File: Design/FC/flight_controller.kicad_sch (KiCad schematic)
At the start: 43 parts, among them U1 STM32H747BIT6

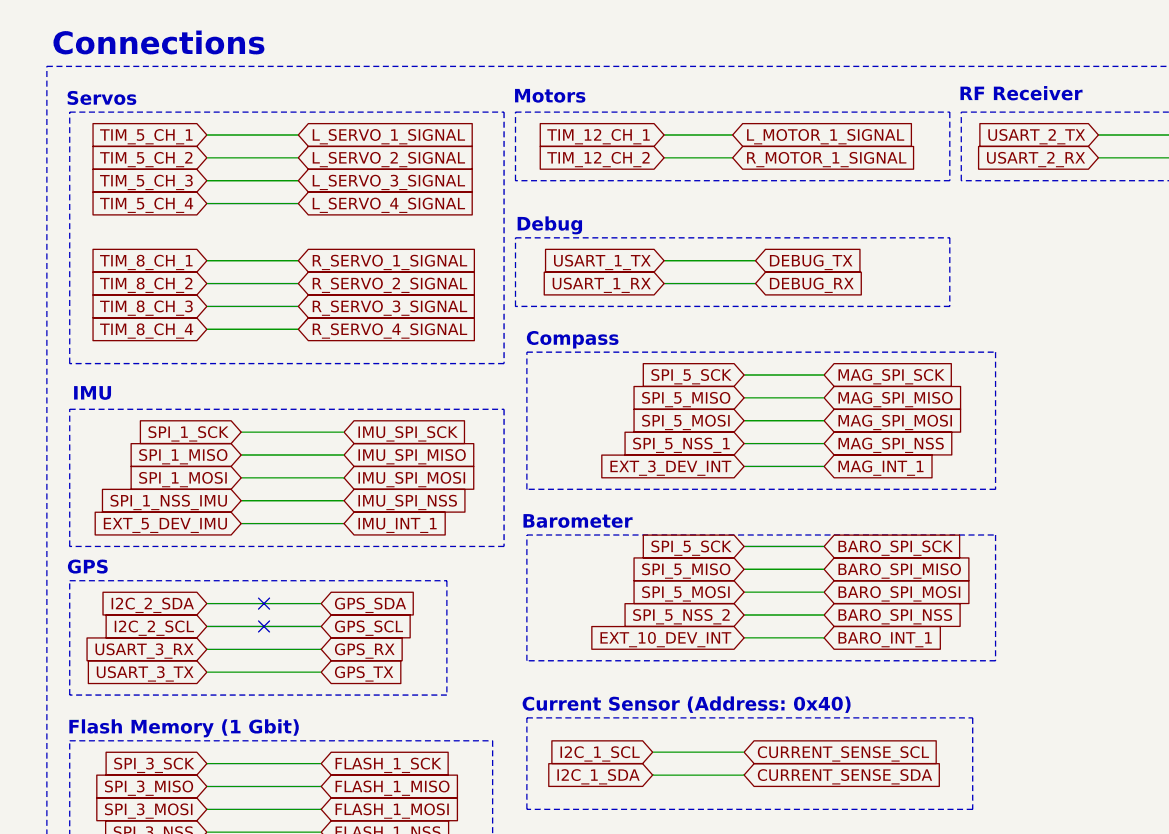
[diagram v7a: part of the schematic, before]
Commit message: extended smd pads for lga packages
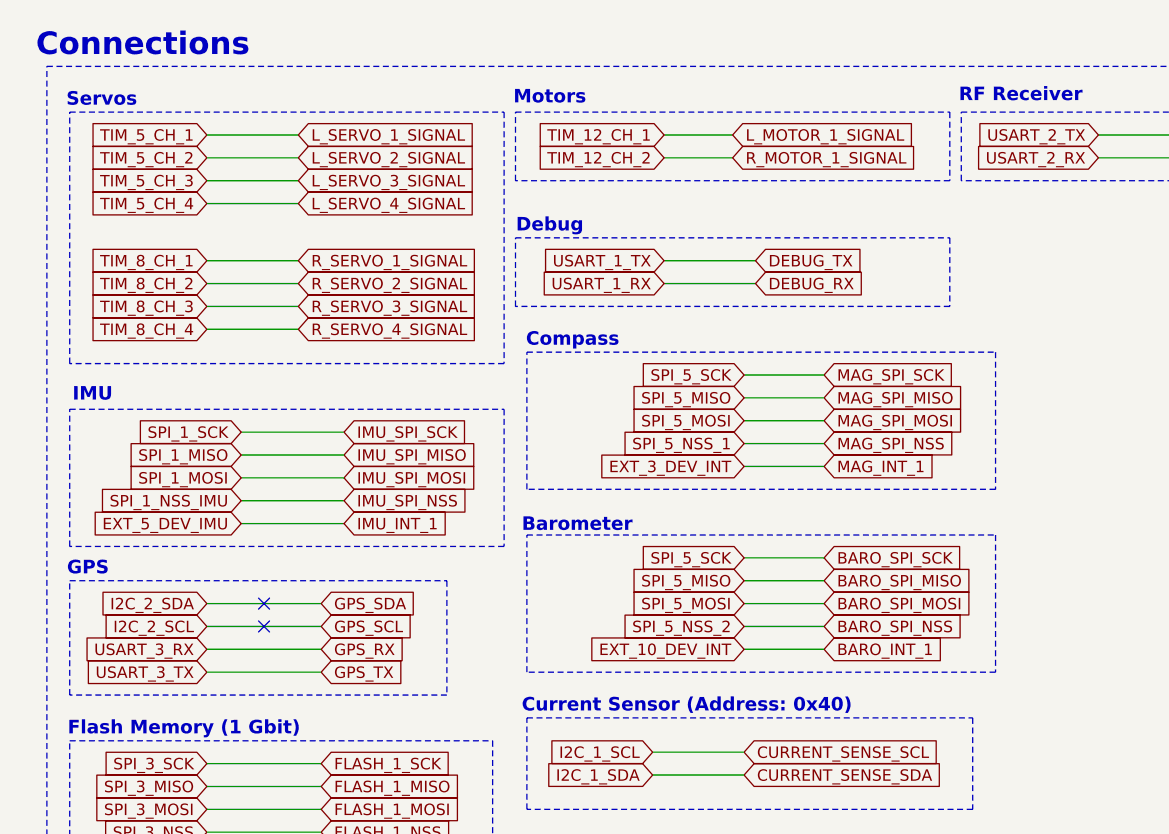
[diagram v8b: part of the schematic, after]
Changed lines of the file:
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@@
 	(rectangle
 		(start 67.31 71.12)
-		(end 119.38 85.09)
+		(end 119.38 86.36)
 		(stroke
 			(width 0)
@@
 	(text "Connections"
 		(exclude_from_sim no)
-		(at 26.416 16.764 0)
+		(at 24.638 16.764 0)
 		(effects
 			(font
@@
 	(text "Barometer"
 		(exclude_from_sim no)
-		(at 72.898 69.85 0)
+		(at 72.898 70.104 0)
 		(effects
 			(font
@@
 	(wire
 		(pts
-			(xy 91.44 74.93) (xy 100.33 74.93)
+			(xy 91.44 76.2) (xy 100.33 76.2)
 		)
 		(stroke
@@
 	(wire
 		(pts
-			(xy 91.44 72.39) (xy 100.33 72.39)
+			(xy 91.44 73.66) (xy 100.33 73.66)
 		)
 		(stroke
@@
 	(wire
 		(pts
-			(xy 91.44 80.01) (xy 100.33 80.01)
+			(xy 91.44 81.28) (xy 100.33 81.28)
 		)
 		(stroke
@@
 	(wire
 		(pts
-			(xy 91.44 77.47) (xy 100.33 77.47)
+			(xy 91.44 78.74) (xy 100.33 78.74)
 		)
 		(stroke
@@
 	(wire
 		(pts
-			(xy 91.44 82.55) (xy 100.33 82.55)
+			(xy 91.44 83.82) (xy 100.33 83.82)
 		)
 		(stroke
@@
 	(global_label "BARO_INT_1"
 		(shape input)
-		(at 100.33 82.55 0)
+		(at 100.33 83.82 0)
 		(fields_autoplaced yes)
 		(effects
@@
 		)
 		(property "Intersheetrefs" "${INTERSHEET_REFS}"
-			(at 114.3219 82.55 0)
+			(at 114.3219 83.82 0)
 			(effects
 				(font
@@
 	(global_label "BARO_SPI_SCK"
 		(shape input)
-		(at 100.33 72.39 0)
+		(at 100.33 73.66 0)
 		(fields_autoplaced yes)
 		(effects
@@
 		)
 		(property "Intersheetrefs" "${INTERSHEET_REFS}"
-			(at 117.0433 72.39 0)
+			(at 117.0433 73.66 0)
 			(effects
 				(font
@@
 	(global_label "EXT_10_DEV_INT"
 		(shape input)
-		(at 91.44 82.55 180)
+		(at 91.44 83.82 180)
 		(fields_autoplaced yes)
 		(effects
@@
 		)
 		(property "Intersheetrefs" "${INTERSHEET_REFS}"
-			(at 73.3964 82.55 0)
+			(at 73.3964 83.82 0)
 			(effects
 				(font
@@
 	(global_label "SPI_5_SCK"
 		(shape input)
-		(at 91.44 72.39 180)
+		(at 91.44 73.66 180)
 		(fields_autoplaced yes)
 		(effects
@@
 		)
 		(property "Intersheetrefs" "${INTERSHEET_REFS}"
-			(at 78.4763 72.39 0)
+			(at 78.4763 73.66 0)
 			(effects
 				(font
@@
 	(global_label "SPI_5_MISO"
 		(shape input)
-		(at 91.44 74.93 180)
+		(at 91.44 76.2 180)
 		(fields_autoplaced yes)
 		(effects
@@
 		)
 		(property "Intersheetrefs" "${INTERSHEET_REFS}"
-			(at 77.6296 74.93 0)
+			(at 77.6296 76.2 0)
 			(effects
 				(font
@@
 	(global_label "BARO_SPI_MISO"
 		(shape input)
-		(at 100.33 74.93 0)
+		(at 100.33 76.2 0)
 		(fields_autoplaced yes)
 		(effects
@@
 		)
 		(property "Intersheetrefs" "${INTERSHEET_REFS}"
-			(at 117.89 74.93 0)
+			(at 117.89 76.2 0)
 			(effects
 				(font
@@
 	(global_label "BARO_SPI_MOSI"
 		(shape input)
-		(at 100.33 77.47 0)
+		(at 100.33 78.74 0)
 		(fields_autoplaced yes)
 		(effects
@@
 		)
 		(property "Intersheetrefs" "${INTERSHEET_REFS}"
-			(at 117.89 77.47 0)
+			(at 117.89 78.74 0)
 			(effects
 				(font
@@
 	(global_label "SPI_5_MOSI"
 		(shape input)
-		(at 91.44 77.47 180)
+		(at 91.44 78.74 180)
 		(fields_autoplaced yes)
 		(effects
@@
 		)
 		(property "Intersheetrefs" "${INTERSHEET_REFS}"
-			(at 77.6296 77.47 0)
+			(at 77.6296 78.74 0)
 			(effects
 				(font
@@
 	(global_label "SPI_5_NSS_2"
 		(shape input)
-		(at 91.44 80.01 180)
+		(at 91.44 81.28 180)
 		(fields_autoplaced yes)
 		(effects
@@
 		)
 		(property "Intersheetrefs" "${INTERSHEET_REFS}"
-			(at 76.2992 80.01 0)
+			(at 76.2992 81.28 0)
 			(effects
 				(font
@@
 	(global_label "BARO_SPI_NSS"
 		(shape input)
-		(at 100.33 80.01 0)
+		(at 100.33 81.28 0)
 		(fields_autoplaced yes)
 		(effects
@@
 		)
 		(property "Intersheetrefs" "${INTERSHEET_REFS}"
-			(at 117.0433 80.01 0)
+			(at 117.0433 81.28 0)
 			(effects
 				(font
